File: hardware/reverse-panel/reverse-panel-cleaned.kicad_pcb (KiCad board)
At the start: 2 copper layers, 116 x 102 mm, 120 parts

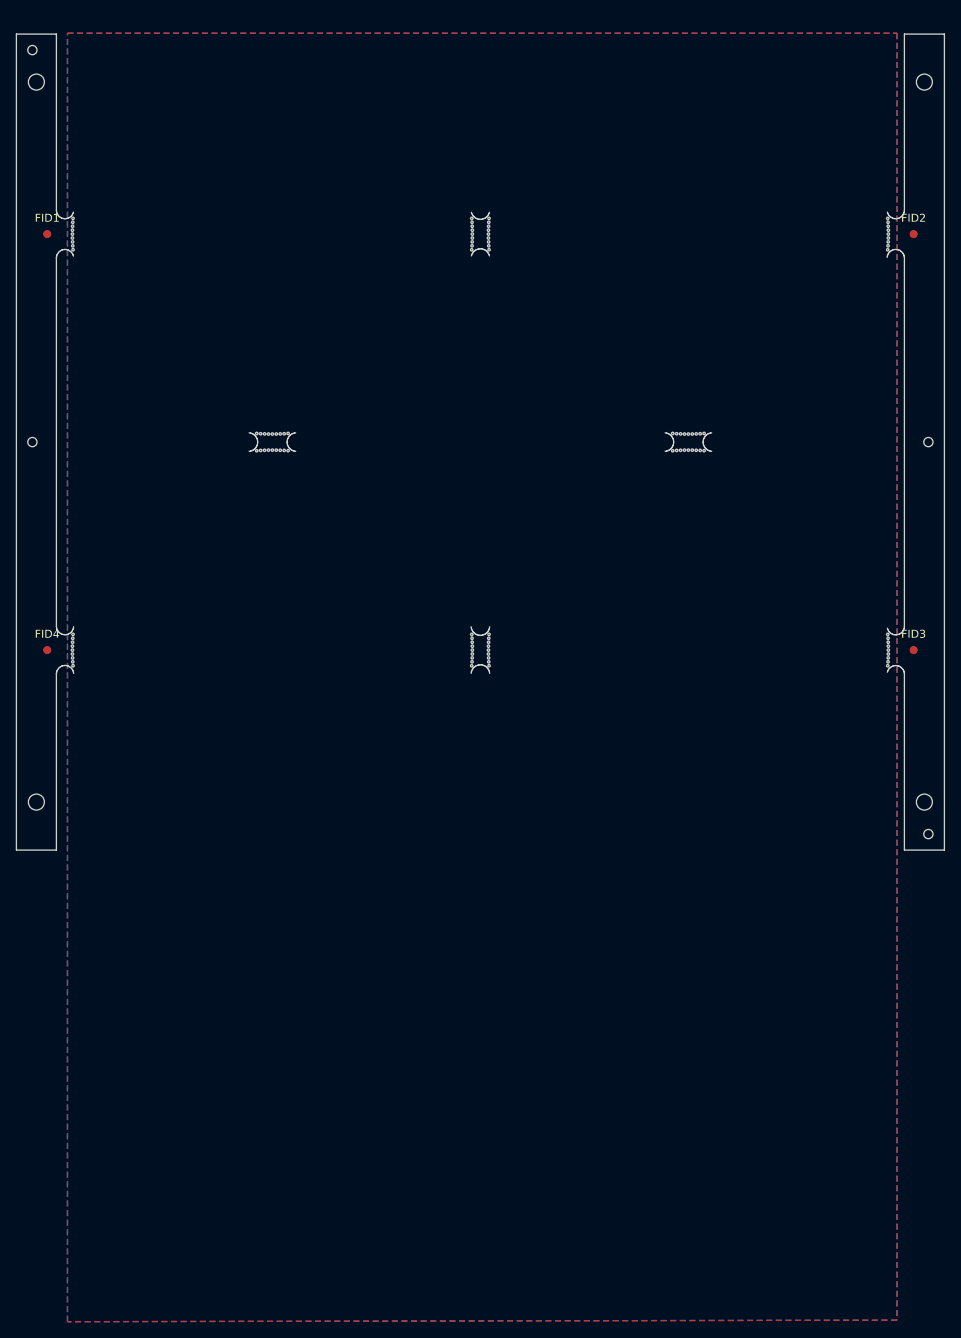
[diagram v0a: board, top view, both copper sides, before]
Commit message: add tooling holes; relocate fiducials
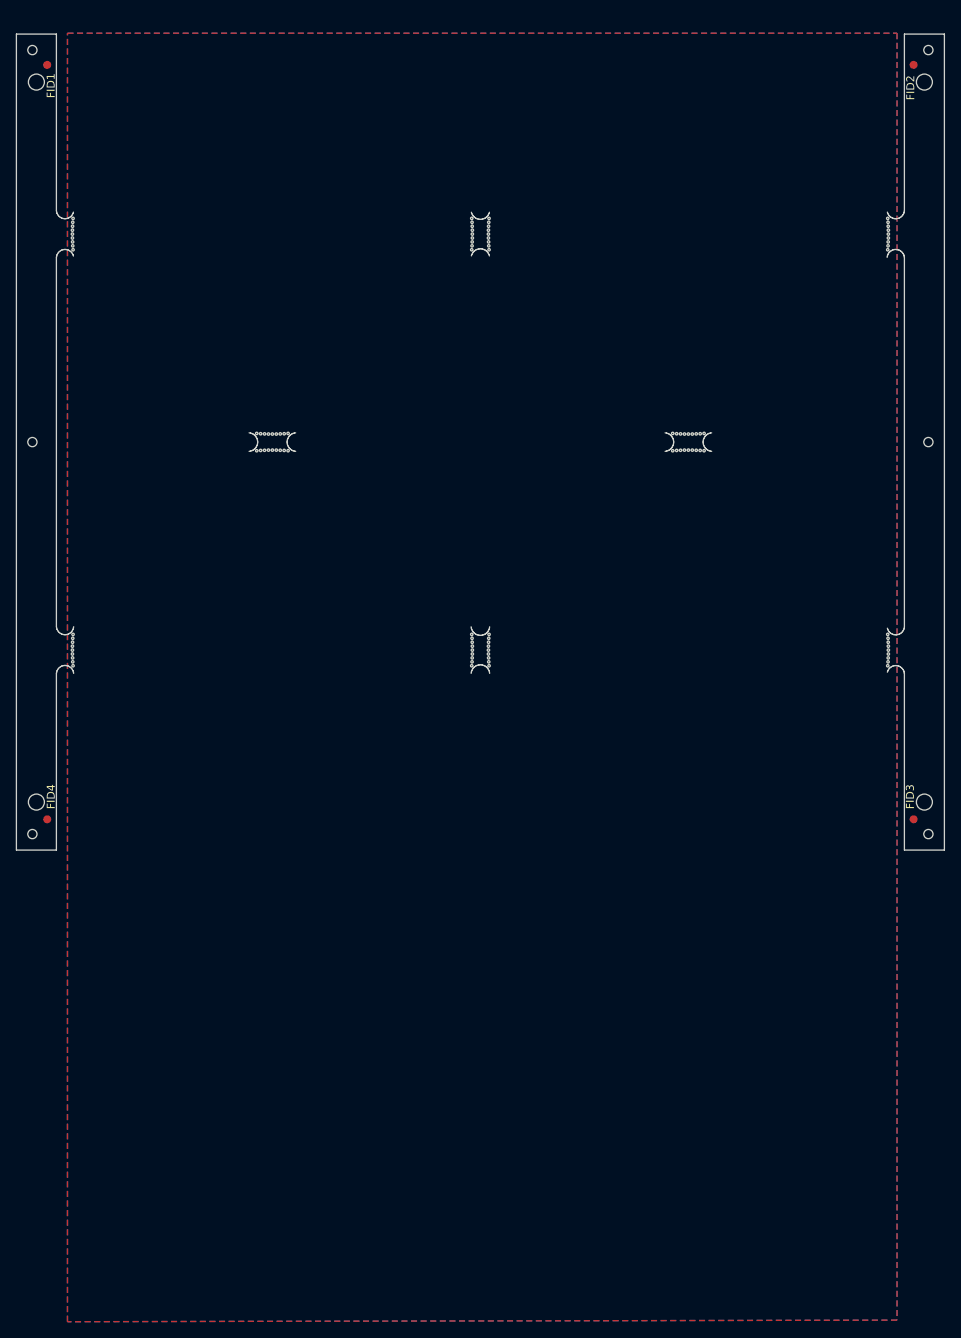
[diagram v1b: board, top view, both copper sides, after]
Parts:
- added ?: , , F.Cu at (132.0, 27.0)
- added ?: , , F.Cu at (20.0, 125.0)
- moved FID3 21.2 mm to (130.2, 123.2)
- moved FID4 21.2 mm to (21.9, 123.2)
- moved FID1 21.1 mm to (21.9, 28.9)
- moved FID2 21.1 mm to (130.2, 28.9)
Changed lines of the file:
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@@
 	(footprint "Fiducial:Fiducial_1mm_Mask2mm"
 		(layer "F.Cu")
-		(at 130.15 102)
+		(at 130.15 123.15)
 		(descr "Circular Fiducial, 1mm bare copper, 2mm soldermask opening (Level A)")
 		(tags "fiducial")
 		(property "Reference" "FID3"
-			(at 0 -2 0)
+			(at -0.43 -2.82 90)
 			(layer "F.SilkS")
 			(effects
@@
 		(embedded_fonts no)
 	)
-	(footprint "Fiducial:Fiducial_1mm_Mask2mm"
-		(layer "F.Cu")
-		(at 21.85 50)
-		(descr "Circular Fiducial, 1mm bare copper, 2mm soldermask opening (Level A)")
-		(tags "fiducial")
-		(property "Reference" "FID1"
-			(at 0 -2 0)
-			(layer "F.SilkS")
-			(effects
-				(font
-					(size 1 1)
-					(thickness 0.15)
-				)
-			)
-		)
-		(property "Value" "Fiducial_1mm_Mask2mm"
-			(at 0 2 0)
-			(layer "F.Fab")
-			(hide yes)
-			(effects
-				(font
-					(size 1 1)
-					(thickness 0.15)
-				)
-			)
-		)
-		(property "Datasheet" ""
-			(at 0 0 0)
-			(unlocked yes)
-			(layer "F.Fab")
-			(hide yes)
-			(effects
-				(font
-					(size 1.27 1.27)
-					(thickness 0.15)
-				)
-			)
-		)
-		(property "Description" ""
-			(at 0 0 0)
-			(unlocked yes)
-			(layer "F.Fab")
-			(hide yes)
-			(effects
-				(font
-					(size 1.27 1.27)
-					(thickness 0.15)
-				)
-			)
-		)
-		(attr smd board_only exclude_from_pos_files exclude_from_bom allow_missing_courtyard
-			dnp
-		)
-		(fp_circle
-			(center 0 0)
-			(end 1.25 0)
-			(stroke
-				(width 0.05)
-				(type solid)
-			)
-			(fill no)
-			(layer "F.CrtYd")
-		)
-		(fp_circle
-			(center 0 0)
-			(end 1 0)
-			(stroke
-				(width 0.1)
-				(type solid)
-			)
-			(fill no)
-			(layer "F.Fab")
-		)
-		(fp_text user "${REFERENCE}"
-			(at 0 0 0)
-			(layer "F.Fab")
-			(effects
-				(font
-					(size 0.4 0.4)
-					(thickness 0.06)
-				)
-			)
-		)
-		(pad "" smd circle
-			(at 0 0)
-			(size 1 1)
-			(layers "F.Cu" "F.Mask")
-			(solder_mask_margin 0.5)
-			(clearance 0.5)
-		)
-		(embedded_fonts no)
-	)
 	(footprint ""
 		(layer "F.Cu")
@@
 		(embedded_fonts no)
 	)
+	(footprint "Fiducial:Fiducial_1mm_Mask2mm"
+		(layer "F.Cu")
+		(at 21.85 28.85)
+		(descr "Circular Fiducial, 1mm bare copper, 2mm soldermask opening (Level A)")
+		(tags "fiducial")
+		(property "Reference" "FID1"
+			(at 0.47 2.6 90)
+			(layer "F.SilkS")
+			(effects
+				(font
+					(size 1 1)
+					(thickness 0.15)
+				)
+			)
+		)
+		(property "Value" "Fiducial_1mm_Mask2mm"
+			(at 0 2 0)
+			(layer "F.Fab")
+			(hide yes)
+			(effects
+				(font
+					(size 1 1)
+					(thickness 0.15)
+				)
+			)
+		)
+		(property "Datasheet" ""
+			(at 0 0 0)
+			(unlocked yes)
+			(layer "F.Fab")
+			(hide yes)
+			(effects
+				(font
+					(size 1.27 1.27)
+					(thickness 0.15)
+				)
+			)
+		)
+		(property "Description" ""
+			(at 0 0 0)
+			(unlocked yes)
+			(layer "F.Fab")
+			(hide yes)
+			(effects
+				(font
+					(size 1.27 1.27)
+					(thickness 0.15)
+				)
+			)
+		)
+		(attr smd board_only exclude_from_pos_files exclude_from_bom allow_missing_courtyard
+			dnp
+		)
+		(fp_circle
+			(center 0 0)
+			(end 1.25 0)
+			(stroke
+				(width 0.05)
+				(type solid)
+			)
+			(fill no)
+			(layer "F.CrtYd")
+		)
+		(fp_circle
+			(center 0 0)
+			(end 1 0)
+			(stroke
+				(width 0.1)
+				(type solid)
+			)
+			(fill no)
+			(layer "F.Fab")
+		)
+		(fp_text user "${REFERENCE}"
+			(at 0 0 0)
+			(layer "F.Fab")
+			(effects
+				(font
+					(size 0.4 0.4)
+					(thickness 0.06)
+				)
+			)
+		)
+		(pad "" smd circle
+			(at 0 0)
+			(size 1 1)
+			(layers "F.Cu" "F.Mask")
+			(solder_mask_margin 0.5)
+			(clearance 0.5)
+		)
+		(embedded_fonts no)
+	)
 	(footprint ""
 		(layer "F.Cu")
@@
 	(footprint ""
 		(layer "F.Cu")
+		(at 132 27)
+		(property "Reference" ""
+			(at 0 0 0)
+			(layer "F.SilkS")
+			(effects
+				(font
+					(size 1.27 1.27)
+					(thickness 0.15)
+				)
+			)
+		)
+		(property "Value" ""
+			(at 0 0 0)
+			(layer "F.Fab")
+			(effects
+				(font
+					(size 1.27 1.27)
+					(thickness 0.15)
+				)
+			)
+		)
+		(property "Datasheet" ""
+			(at 0 0 0)
+			(layer "F.Fab")
+			(hide yes)
+			(effects
+				(font
+					(size 1.27 1.27)
+					(thickness 0.15)
+				)
+			)
+		)
+		(property "Description" ""
+			(at 0 0 0)
+			(layer "F.Fab")
+			(hide yes)
+			(effects
+				(font
+					(size 1.27 1.27)
+					(thickness 0.15)
+				)
+			)
+		)
+		(attr board_only exclude_from_pos_files exclude_from_bom allow_missing_courtyard
+			dnp
+		)
+		(pad "" np_thru_hole circle
+			(at 0 0 90)
+			(size 1.152 1.152)
+			(drill 1.152)
+			(layers "*.Cu" "*.Mask")
+			(pinfunction "Pin_2")
+			(pintype "passive")
+			(solder_mask_margin 0.148)
+			(solder_paste_margin 1.152)
+		)
+		(embedded_fonts no)
+	)
+	(footprint ""
+		(layer "F.Cu")
 		(at 20 76)
 		(property "Reference" ""
@@
 		(embedded_fonts no)
 	)
+	(footprint ""
+		(layer "F.Cu")
+		(at 20 125)
+		(property "Reference" ""
+			(at 0 0 0)
+			(layer "F.SilkS")
+			(effects
+				(font
+					(size 1.27 1.27)
+					(thickness 0.15)
+				)
+			)
+		)
+		(property "Value" ""
+			(at 0 0 0)
+			(layer "F.Fab")
+			(effects
+				(font
+					(size 1.27 1.27)
+					(thickness 0.15)
+				)
+			)
+		)
+		(property "Datasheet" ""
+			(at 0 0 0)
+			(layer "F.Fab")
+			(hide yes)
+			(effects
+				(font
+					(size 1.27 1.27)
+					(thickness 0.15)
+				)
+			)
+		)
+		(property "Description" ""
+			(at 0 0 0)
+			(layer "F.Fab")
+			(hide yes)
+			(effects
+				(font
+					(size 1.27 1.27)
+					(thickness 0.15)
+				)
+			)
+		)
+		(attr board_only exclude_from_pos_files exclude_from_bom allow_missing_courtyard
+			dnp
+		)
+		(pad "" np_thru_hole circle
+			(at 0 0 90)
+			(size 1.152 1.152)
+			(drill 1.152)
+			(layers "*.Cu" "*.Mask")
+			(pinfunction "Pin_2")
+			(pintype "passive")
+			(solder_mask_margin 0.148)
+			(solder_paste_margin 1.152)
+		)
+		(embedded_fonts no)
+	)
 	(footprint "Fiducial:Fiducial_1mm_Mask2mm"
 		(layer "F.Cu")
-		(at 130.15 50)
+		(at 130.15 28.85)
 		(descr "Circular Fiducial, 1mm bare copper, 2mm soldermask opening (Level A)")
 		(tags "fiducial")
 		(property "Reference" "FID2"
-			(at 0 -2 0)
+			(at -0.38 2.86 90)
 			(layer "F.SilkS")
 			(effects
@@
 	(footprint "Fiducial:Fiducial_1mm_Mask2mm"
 		(layer "F.Cu")
-		(at 21.85 102)
+		(at 21.85 123.15)
 		(descr "Circular Fiducial, 1mm bare copper, 2mm soldermask opening (Level A)")
 		(tags "fiducial")
 		(property "Reference" "FID4"
-			(at 0 -2 0)
+			(at 0.48 -2.82 90)
 			(layer "F.SilkS")
 			(effects

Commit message: add tooling holes; relocate fiducials; cleanup
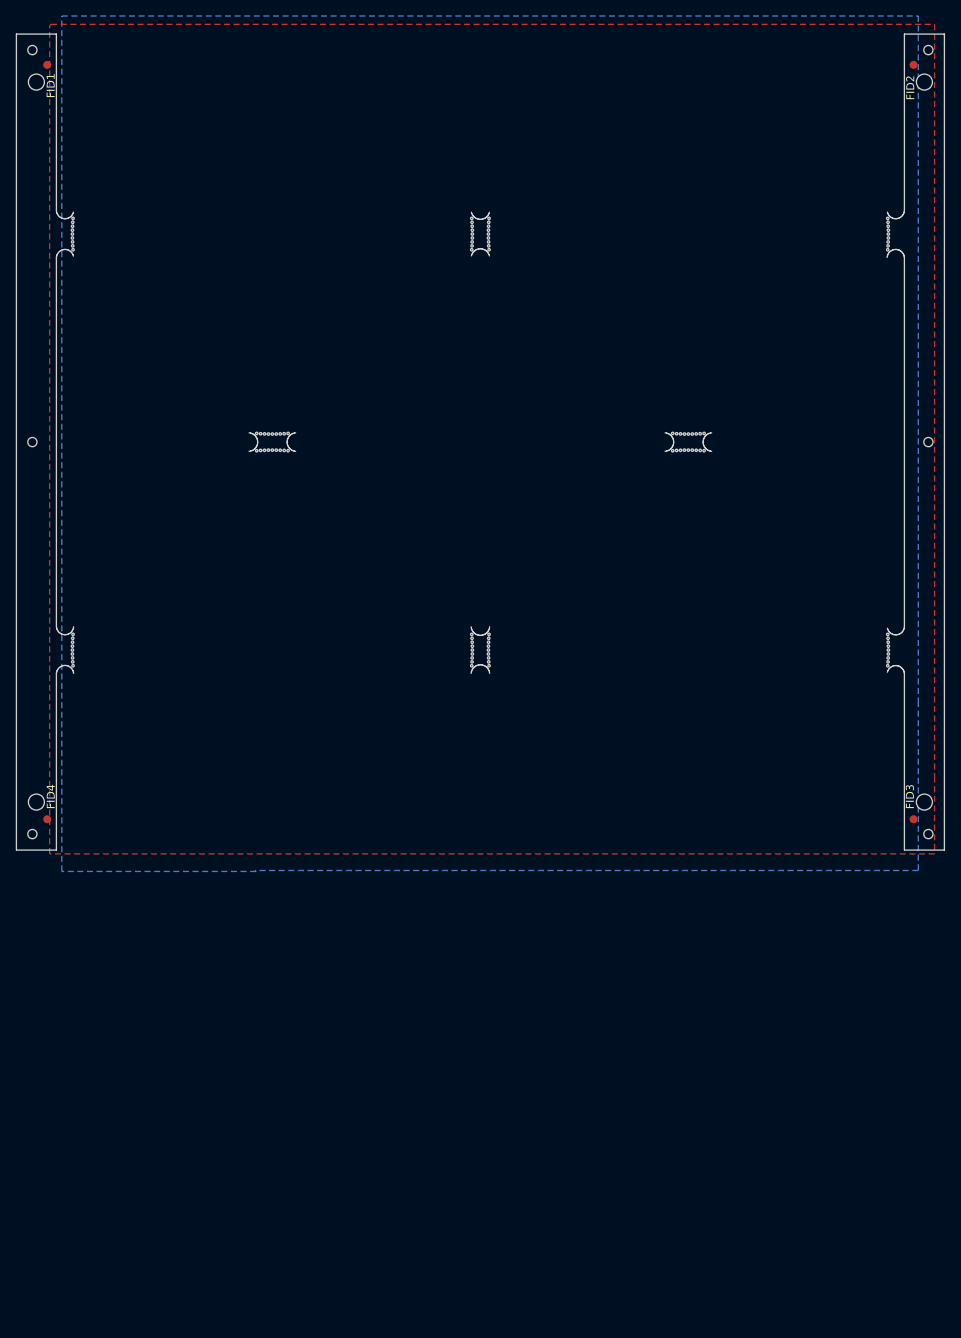
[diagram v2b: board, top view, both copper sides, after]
